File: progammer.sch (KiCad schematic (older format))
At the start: 58 parts, among them J5 USB_B_Micro, U1 ICE40HX4K-TQ144, U11 TXS0108EPW, U13 TXS0108EPW, U14 MIC5365-3.3YC5, U3 93LCxxBT-I_OT, U4 FT2232H, U5 IS25LP080D, Y1 ECS-3225S33-120-FN-TR

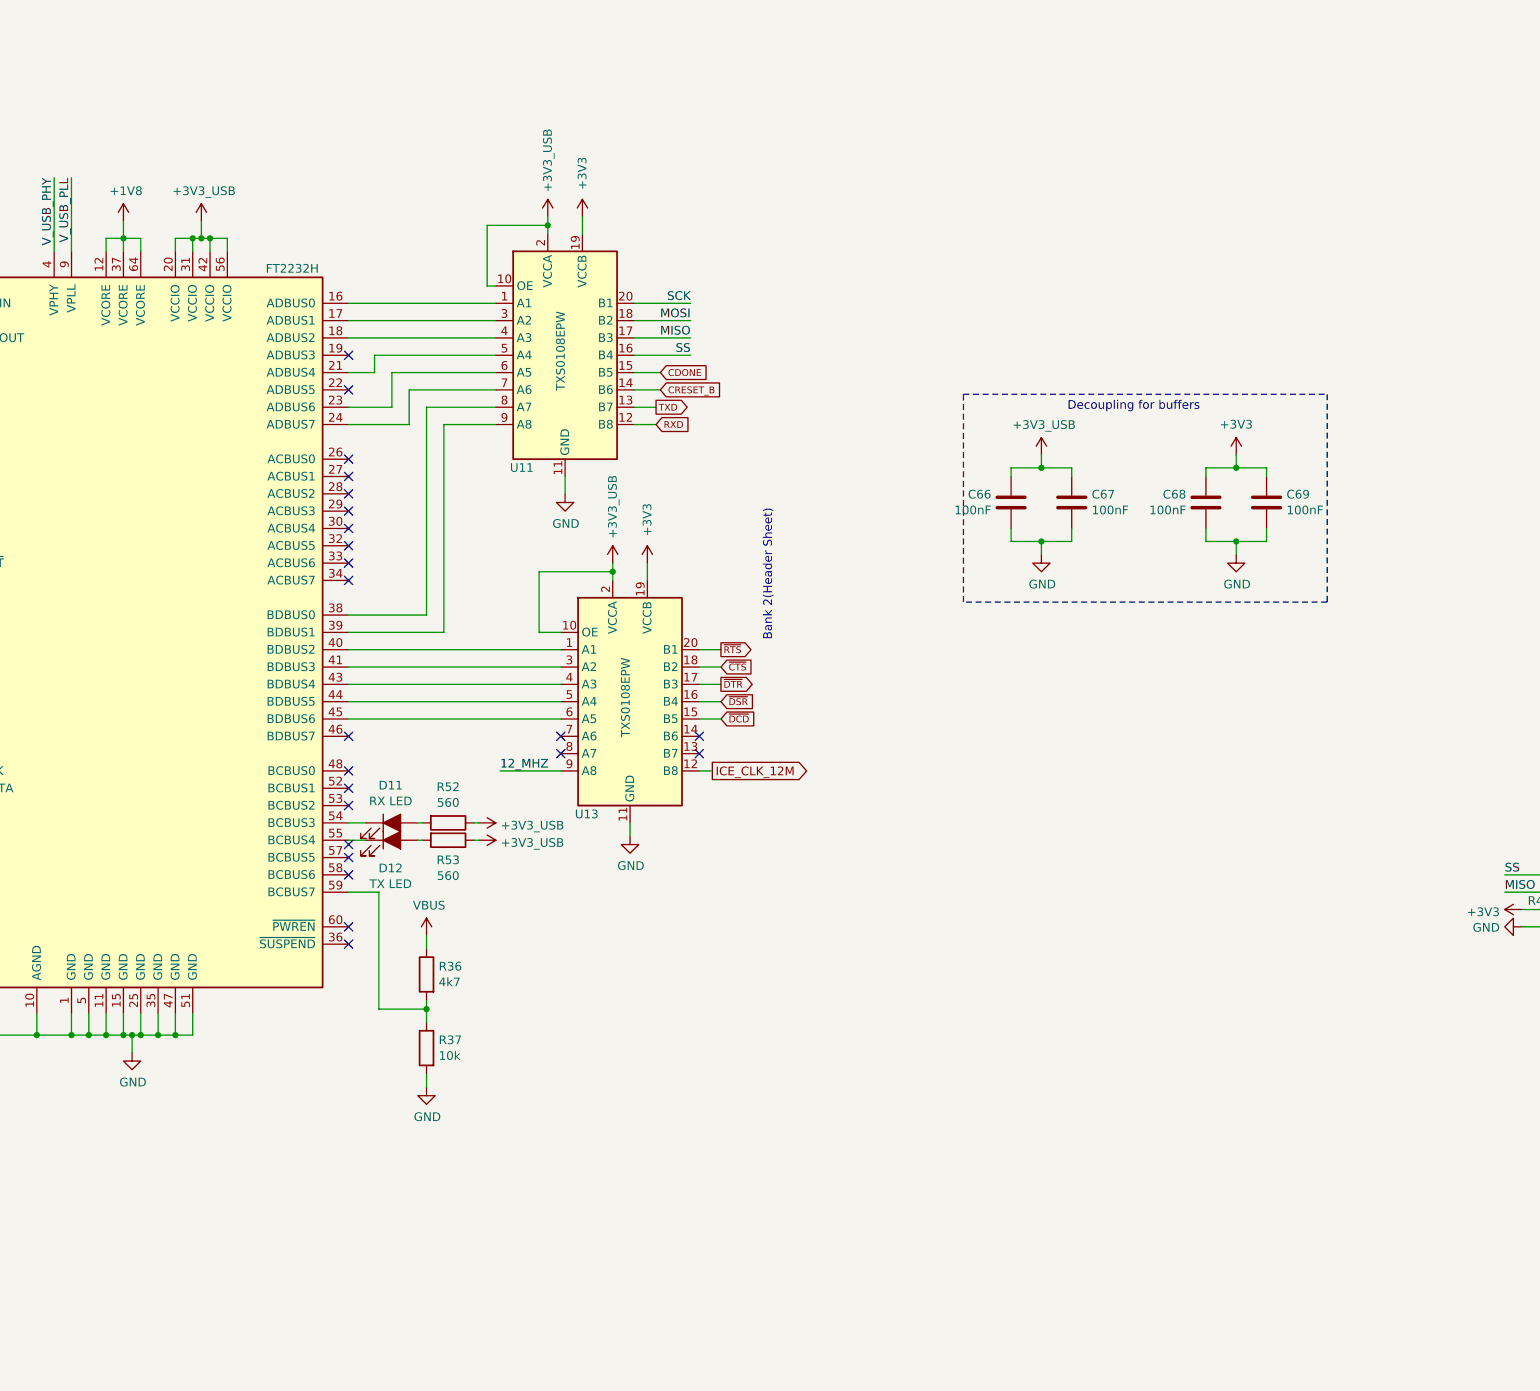
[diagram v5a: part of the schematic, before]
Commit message: Implemented proper Powerseparation between FTDI and FPGA. The old solution may not work correctly
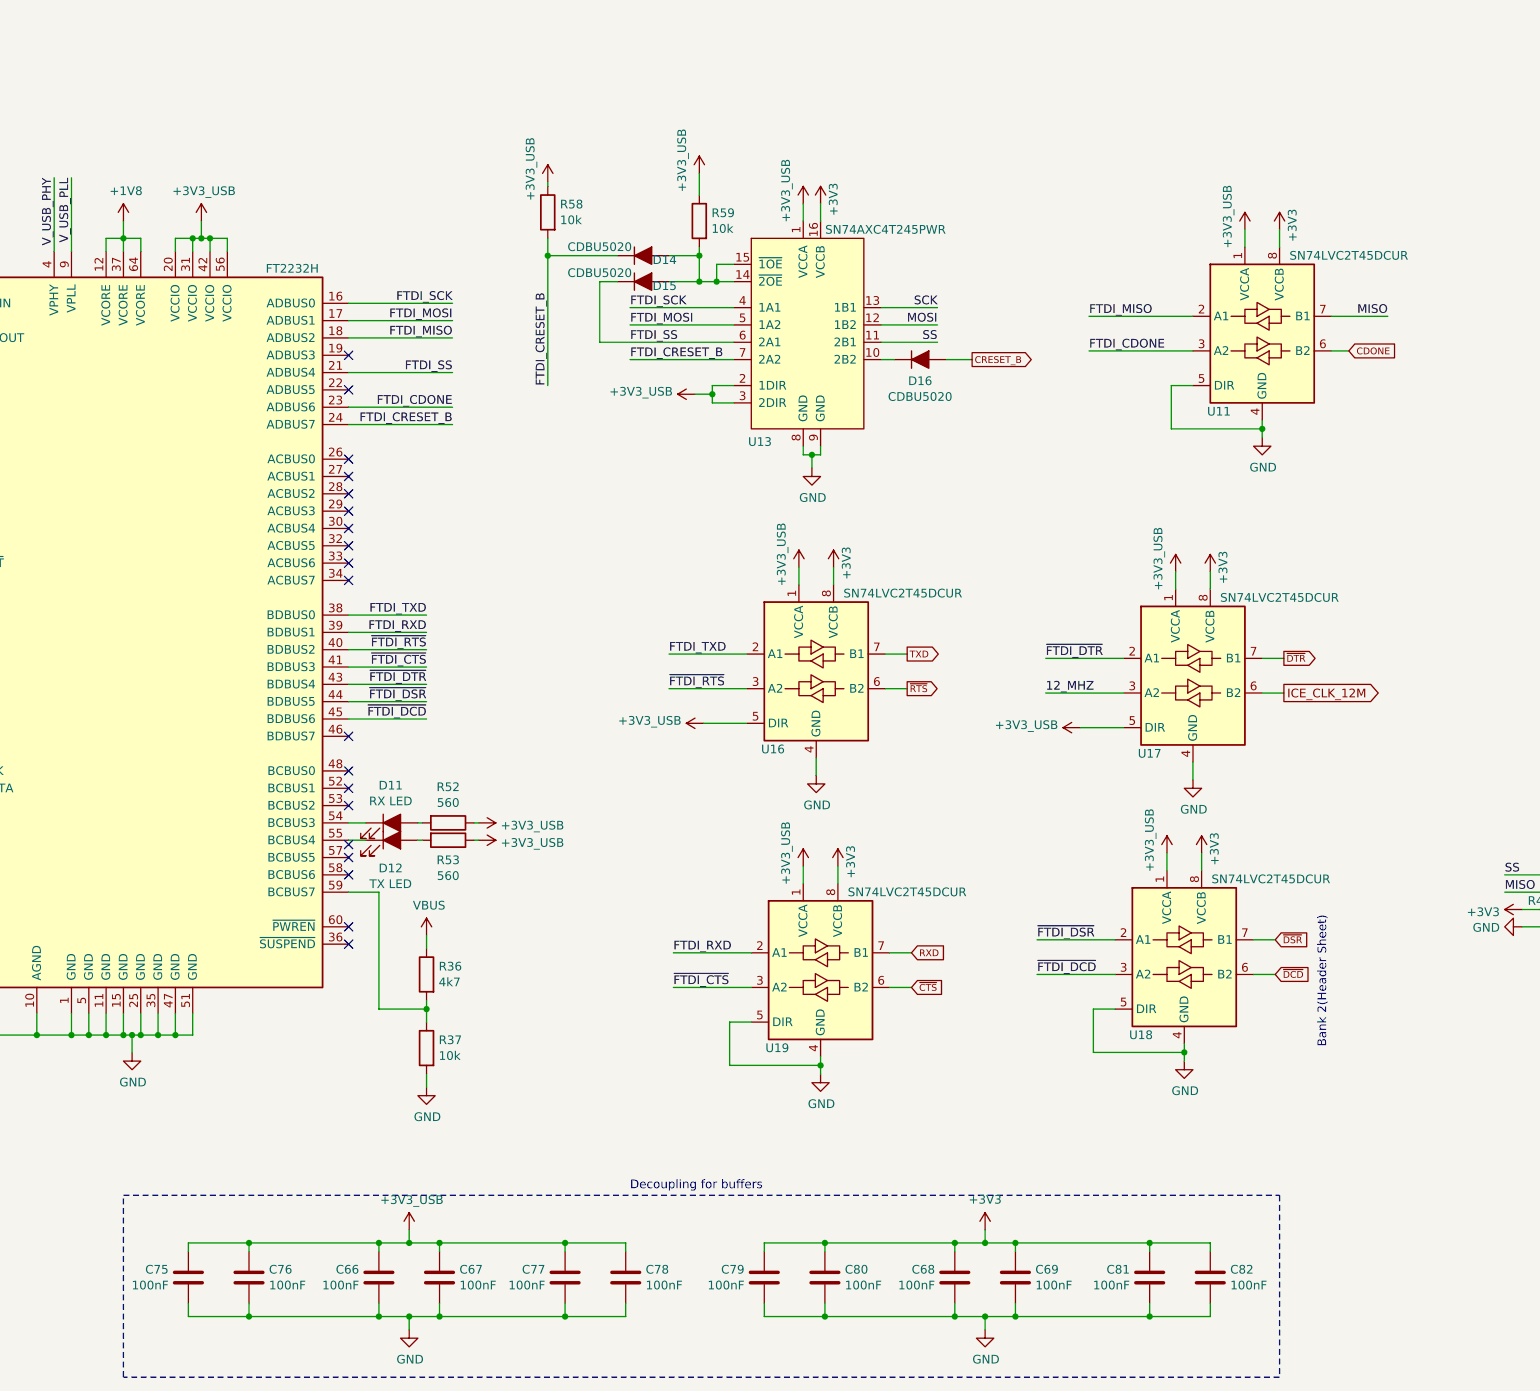
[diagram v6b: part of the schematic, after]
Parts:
- removed U11, U13: TXS0108EPW, Package_SO:TSSOP-20_4.4x6.5mm_P0.65mm, symbol Logic_LevelTranslator:TXS0108EPW
- added C75, C76, C77, C78, C79, C80, C81, C82: 100nF, Capacitor_SMD:C_0603_1608Metric, symbol Device:C
- added D14, D15, D16: CDBU5020, Diode_SMD:D_0603_1608Metric, symbol Device:D_ALT
- added R58, R59: 10k, Resistor_SMD:R_0603_1608Metric, symbol Device:R
- added U11, U16, U17, U18, U19: SN74LVC2T45DCUR, Package_SO:VSSOP-8_2.4x2.1mm_P0.5mm, symbol Logic_LevelTranslator:SN74LVC2T45DCUR
- added U13: SN74AXC4T245PWR, Package_SO:TSSOP-16_4.4x5mm_P0.65mm, symbol SN74AXC4T245PWR:SN74AXC4T245PWR
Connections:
- net +3V3: now also C79.1, C80.1, C81.1, C82.1, U11.8 (VCCB), U13.16 (VCCB), U16.8 (VCCB), U17.8 (VCCB), U18.8 (VCCB), U19.8 (VCCB)
- net +3V3_FTDI: now also C75.1, C76.1, C77.1, C78.1, R58.1, R59.1, U11.1 (VCCA), U13.1 (VCCA), U13.2 (1DIR), U13.3 (2DIR), U16.1 (VCCA), U16.5 (DIR), U17.1 (VCCA), U17.5 (DIR), U18.1 (VCCA), U19.1 (VCCA)
- net 12_MHZ: now also U17.3 (A2)
- net CDONE: now also U11.6 (B2)
- net CRESET_B: now also D16.2 (A)
- net GND: now also C75.2, C76.2, C77.2, C78.2, C79.2, C80.2, C81.2, C82.2, U11.4 (GND), U11.5 (DIR), U13.8 (GND), U13.9 (GND), U16.4 (GND), U17.4 (GND), U18.4 (GND), U18.5 (DIR), U19.4 (GND), U19.5 (DIR)
- net ICE_CLK_12M: now also U17.6 (B2)
- net MISO: now also U11.7 (B1)
- net MOSI: now also U13.12 (1B2)
- net RXD: now also U19.7 (B1)
- net SCK: now also U13.13 (1B1)
- net SS: now also U13.11 (2B1)
- net TXD: now also U16.7 (B1)
- net ~CTS~: now also U19.6 (B2)
- net ~DCD~: now also U18.6 (B2)
- net ~DSR~: now also U18.7 (B1)
- net ~DTR~: now also U17.7 (B1)
- net ~RTS~: now also U16.6 (B2)
- net FTDI_SCK: now reaches U4.16 (ADBUS0)
- net FTDI_SCK: now also U13.4 (1A1)
- net FTDI_MOSI: now reaches U4.17 (ADBUS1)
- net FTDI_MOSI: now also U13.5 (1A2)
- net FTDI_MISO: now reaches U4.18 (ADBUS2)
- net FTDI_MISO: now also U11.2 (A1)
- net FTDI_SS: now reaches U4.21 (ADBUS4)
- net FTDI_SS: now also D15.1 (K), U13.6 (2A1)
- net FTDI_CDONE: now reaches U4.23 (ADBUS6)
- net FTDI_CDONE: now also U11.3 (A2)
- net FTDI_CRESET_B: now reaches U4.24 (ADBUS7)
- net FTDI_CRESET_B: now also D14.1 (K), R58.2, U13.7 (2A2)
- net FTDI_TXD: now reaches U4.38 (BDBUS0)
- net FTDI_TXD: now also U16.2 (A1)
- net FTDI_RXD: now reaches U4.39 (BDBUS1)
- net FTDI_RXD: now also U19.2 (A1)
- net ~FTDI_RTS~: now reaches U4.40 (BDBUS2)
- net ~FTDI_RTS~: now also U16.3 (A2)
- net ~FTDI_CTS~: now reaches U4.41 (BDBUS3)
- net ~FTDI_CTS~: now also U19.3 (A2)
- net ~FTDI_DTR~: now reaches U4.43 (BDBUS4)
- net ~FTDI_DTR~: now also U17.2 (A1)
- net ~FTDI_DSR~: now reaches U4.44 (BDBUS5)
- net ~FTDI_DSR~: now also U18.2 (A1)
- net ~FTDI_DCD~: now reaches U4.45 (BDBUS6)
- net ~FTDI_DCD~: now also U18.3 (A2)
- new net: D16.1 (K), U13.10 (2B2)
- new net: D14.2 (A), D15.2 (A), R59.2, U13.14 (~2OE~), U13.15 (~1OE~)
- no-connect marks 27 -> 23
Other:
- moved on the sheet: C66, C67, C68, C69

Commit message: Continued on routing
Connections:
- net 12_MHZ: now also U17.2 (A1); no longer U17.3 (A2)
- net CDONE: now also U11.7 (B1); no longer U11.6 (B2)
- net FTDI_CDONE: now also U11.2 (A1); no longer U11.3 (A2)
- net FTDI_CRESET_B: now also U13.4 (1A1); no longer U13.7 (2A2)
- net FTDI_MISO: now also U11.3 (A2); no longer U11.2 (A1)
- net FTDI_MOSI: now also U13.6 (2A1); no longer U13.5 (1A2)
- net FTDI_RXD: now also U19.3 (A2); no longer U19.2 (A1)
- net FTDI_SCK: now also U13.7 (2A2); no longer U13.4 (1A1)
- net FTDI_SS: now also U13.5 (1A2); no longer U13.6 (2A1)
- net FTDI_TXD: now also U16.3 (A2); no longer U16.2 (A1)
- net ICE_CLK_12M: now also U17.7 (B1); no longer U17.6 (B2)
- net MISO: now also U11.6 (B2); no longer U11.7 (B1)
- net MOSI: now also U13.11 (2B1); no longer U13.12 (1B2)
- net RXD: now also U19.6 (B2); no longer U19.7 (B1)
- net SCK: now also U13.10 (2B2); no longer U13.13 (1B1)
- net SS: now also U13.12 (1B2); no longer U13.11 (2B1)
- net TXD: now also U16.6 (B2); no longer U16.7 (B1)
- net ~CTS~: now also U19.7 (B1); no longer U19.6 (B2)
- net ~DCD~: now also U18.7 (B1); no longer U18.6 (B2)
- net ~DSR~: now also U18.6 (B2); no longer U18.7 (B1)
- net ~DTR~: now also U17.6 (B2); no longer U17.7 (B1)
- net ~FTDI_CTS~: now also U19.2 (A1); no longer U19.3 (A2)
- net ~FTDI_DCD~: now also U18.2 (A1); no longer U18.3 (A2)
- net ~FTDI_DSR~: now also U18.3 (A2); no longer U18.2 (A1)
- net ~FTDI_DTR~: now also U17.3 (A2); no longer U17.2 (A1)
- net ~FTDI_RTS~: now also U16.2 (A1); no longer U16.3 (A2)
- net ~RTS~: now also U16.7 (B1); no longer U16.6 (B2)
- net at D16.1 (K): now also U13.13 (1B1); no longer U13.10 (2B2)
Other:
- moved on the sheet: D16
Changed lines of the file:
@@
 NoConn ~ 6025 6325
 NoConn ~ 6025 7225
-Text Label 9425 4850 2    50   ~ 0
+Text Label 9575 4950 2    50   ~ 0
 MOSI
-Text Label 9425 4750 2    50   ~ 0
+Text Label 9575 5050 2    50   ~ 0
 SCK
 Wire Wire Line
-	9425 4750 9100 4750
+	9575 5050 9100 5050
 $Comp
 L Device:R R43
@@
 Wire Wire Line
 	14550 7475 14550 7325
+Text GLabel 9250 6950 2    39   Output ~ 0
+TXD
+Text GLabel 9275 8675 2    39   Input ~ 0
+RXD
 Text GLabel 9250 6750 2    39   Output ~ 0
-TXD
-Text GLabel 9275 8475 2    39   Input ~ 0
-RXD
-Text GLabel 9250 6950 2    39   Output ~ 0
 ~RTS~
-Text GLabel 9275 8675 2    39   Input ~ 0
-~CTS~
-Text GLabel 11425 6775 2    39   Output ~ 0
+Text GLabel 11425 6975 2    39   Output ~ 0
 ~DTR~
-Text GLabel 11375 8400 2    39   Input ~ 0
-~DSR~
-Text GLabel 11375 8600 2    39   Input ~ 0
-~DCD~
+Wire Wire Line
+	9125 6950 9250 6950
+Wire Wire Line
+	9275 8675 9150 8675
 Wire Wire Line
 	9125 6750 9250 6750
 Wire Wire Line
-	9275 8475 9150 8475
-Wire Wire Line
-	9125 6950 9250 6950
-Wire Wire Line
-	9275 8675 9150 8675
-Wire Wire Line
-	11300 6775 11425 6775
-Wire Wire Line
-	11375 8400 11250 8400
-Wire Wire Line
-	11250 8600 11375 8600
+	11300 6975 11425 6975
 $Comp
 L Device:LED_ALT D?
@@
 Text Notes 11675 9025 1    50   ~ 0
 Bank 2(Header Sheet)
-Text GLabel 9625 5050 2    39   Output ~ 0
+Text GLabel 9650 4750 2    39   Output ~ 0
 CRESET_B
 Wire Wire Line
-	9625 5050 9475 5050
-Text GLabel 11425 6975 2    50   Output ~ 0
+	9650 4750 9500 4750
+Text GLabel 11425 6775 2    50   Output ~ 0
 ICE_CLK_12M
 $Comp
@@
 	6025 7125 6475 7125
 Wire Wire Line
-	11425 6975 11300 6975
+	11425 6775 11300 6775
 Text Label 3450 8575 2    50   ~ 0
 12_MHZ
@@
 Wire Wire Line
 	11300 5500 11300 5450
-Text Label 7650 4750 0    50   ~ 0
+Text Label 7650 5050 0    50   ~ 0
 FTDI_SCK
-Text Label 7650 4850 0    50   ~ 0
+Text Label 7650 4950 0    50   ~ 0
 FTDI_MOSI
 Wire Wire Line
-	7650 4750 8250 4750
-Wire Wire Line
-	8250 4850 7650 4850
-Wire Wire Line
-	12025 4800 11700 4800
-Text Label 12025 4800 2    50   ~ 0
+	7650 5050 8250 5050
+Wire Wire Line
+	8250 4950 7650 4950
+Wire Wire Line
+	12025 5000 11700 5000
+Text Label 12025 5000 2    50   ~ 0
 MISO
-Text Label 10300 4800 0    50   ~ 0
+Text Label 10300 5000 0    50   ~ 0
 FTDI_MISO
 Wire Wire Line
-	10300 4800 10900 4800
+	10300 5000 10900 5000
 Wire Wire Line
 	11200 4300 11200 4400
@@
 Wire Wire Line
 	8125 5250 8125 5300
-Text Label 7650 4950 0    50   ~ 0
+Text Label 7650 4850 0    50   ~ 0
 FTDI_SS
-Text Label 9425 4950 2    50   ~ 0
+Text Label 9575 4850 2    50   ~ 0
 SS
 Wire Wire Line
-	9425 4950 9100 4950
-Wire Wire Line
-	9100 4850 9425 4850
-Text Label 7650 5050 0    50   ~ 0
+	9575 4850 9100 4850
+Wire Wire Line
+	9100 4950 9575 4950
+Text Label 7650 4750 0    50   ~ 0
 FTDI_CRESET_B
 Wire Wire Line
-	7650 5050 8250 5050
+	7650 4750 8250 4750
 $Comp
 L Device:R R58
@@
 	7575 4600 7475 4600
 Wire Wire Line
-	7475 4600 7475 4950
-Wire Wire Line
-	7475 4950 8250 4950
+	7475 4850 8250 4850
 $Comp
 L Device:D_ALT D?
@@
 L Device:D_ALT D?
 U 1 1 5F95FFD7
-P 9325 5050
+P 9350 4750
 AR Path="/5CA8FBC7/5F95FFD7" Ref="D?"  Part="1"
 AR Path="/5CAB8B22/5F95FFD7" Ref="D16"  Part="1"
-F 0 "D16" H 9325 4926 50  0000 C CNN
-F 1 "CDBU5020" H 9325 4835 50  0000 C CNN
-F 2 "Diode_SMD:D_0603_1608Metric" H 9325 5050 50  0001 C CNN
-F 3 "http://www.comchiptech.com/admin/files/product/CDBU0520-HF-RevA797161.pdf" H 9325 5050 50  0001 C CNN
-F 4 "Comchip Technology" H 9325 5050 50  0001 C CNN "Mfg Name"
-F 5 "CDBU0520" H 9325 5050 50  0001 C CNN "Mfg Part Num"
-F 6 "641-1332-1-ND" H 9325 5050 50  0001 C CNN "Digikey"
-F 7 "DIODE SCHOTTKY 20V 500MA 0603" H 9325 5050 50  0001 C CNN "Description"
-	1    9325 5050
-	1    0    0    -1
-$EndComp
-Wire Wire Line
-	9175 5050 9100 5050
+F 0 "D16" H 9350 4966 50  0000 C CNN
+F 1 "CDBU5020" H 9350 4875 50  0000 C CNN
+F 2 "Diode_SMD:D_0603_1608Metric" H 9350 4750 50  0001 C CNN
+F 3 "http://www.comchiptech.com/admin/files/product/CDBU0520-HF-RevA797161.pdf" H 9350 4750 50  0001 C CNN
+F 4 "Comchip Technology" H 9350 4750 50  0001 C CNN "Mfg Name"
+F 5 "CDBU0520" H 9350 4750 50  0001 C CNN "Mfg Part Num"
+F 6 "641-1332-1-ND" H 9350 4750 50  0001 C CNN "Digikey"
+F 7 "DIODE SCHOTTKY 20V 500MA 0603" H 9350 4750 50  0001 C CNN "Description"
+	1    9350 4750
+	1    0    0    -1
+$EndComp
+Wire Wire Line
+	9200 4750 9100 4750
 Wire Wire Line
 	10900 5200 10775 5200
@@
 Wire Wire Line
 	11300 5450 11300 5400
-Text Label 10300 5000 0    50   ~ 0
+Text Label 10300 4800 0    50   ~ 0
 FTDI_CDONE
 Wire Wire Line
-	10300 5000 10900 5000
-Text GLabel 11800 5000 2    39   Input ~ 0
-CDONE
-Wire Wire Line
-	11800 5000 11700 5000
+	10300 4800 10900 4800
 Text Label 6475 6525 2    50   ~ 0
 FTDI_TXD
@@
 	8725 7350 8725 7450
 Wire Wire Line
-	8325 6750 7875 6750
-Text Label 7875 6750 0    50   ~ 0
-FTDI_TXD
-Wire Wire Line
 	8325 6950 7875 6950
 Text Label 7875 6950 0    50   ~ 0
-~FTDI_RTS~
+FTDI_TXD
 $Comp
 L power_symbols:+3V3_USB #PWR0177
@@
 Wire Wire Line
 	10250 7175 10500 7175
+Wire Wire Line
+	10500 6975 10050 6975
 Text Label 10050 6975 0    50   ~ 0
-12_MHZ
-Wire Wire Line
-	10050 6975 10500 6975
-Wire Wire Line
-	10500 6775 10050 6775
-Text Label 10050 6775 0    50   ~ 0
 ~FTDI_DTR~
 $Comp
@@
 	8750 9125 8750 9075
 Wire Wire Line
+	8350 8675 7900 8675
+Text Label 7900 8675 0    50   ~ 0
+FTDI_RXD
+Wire Wire Line
 	8350 8475 7900 8475
 Text Label 7900 8475 0    50   ~ 0
-FTDI_RXD
-Wire Wire Line
-	8350 8675 7900 8675
-Text Label 7900 8675 0    50   ~ 0
 ~FTDI_CTS~
 $Comp
@@
 	10850 9050 10850 9000
 Wire Wire Line
+	10450 8600 10000 8600
+Text Label 10000 8600 0    50   ~ 0
+~FTDI_DSR~
+Wire Wire Line
 	10450 8400 10000 8400
 Text Label 10000 8400 0    50   ~ 0
-~FTDI_DSR~
-Wire Wire Line
-	10450 8600 10000 8600
-Text Label 10000 8600 0    50   ~ 0
 ~FTDI_DCD~
 $Comp
@@
 Wire Notes Line
 	4725 9875 11400 9875
+Text GLabel 11800 4800 2    39   Input ~ 0
+CDONE
+Wire Wire Line
+	11800 4800 11700 4800
+Text Label 7875 6750 0    50   ~ 0
+~FTDI_RTS~
+Wire Wire Line
+	8325 6750 7875 6750
+Wire Wire Line
+	10050 6775 10500 6775
+Text Label 10050 6775 0    50   ~ 0
+12_MHZ
+Text GLabel 9275 8475 2    39   Input ~ 0
+~CTS~
+Wire Wire Line
+	9275 8475 9150 8475
+Text GLabel 11375 8600 2    39   Input ~ 0
+~DSR~
+Wire Wire Line
+	11375 8600 11250 8600
+Text GLabel 11375 8400 2    39   Input ~ 0
+~DCD~
+Wire Wire Line
+	11250 8400 11375 8400
+Wire Wire Line
+	7475 4850 7475 4600
 $EndSCHEMATC
